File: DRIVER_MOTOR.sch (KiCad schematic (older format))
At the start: 14 parts, among them J7 MOT ARM, J8 MOT POLE, Q5 BC817, Q6 BC817, Q7 BC817, Q8 BC817

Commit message: cambiado a conectores MOLEX KK, agregados test points para señales analogicas
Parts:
- J3: renamed from J7; footprint Connector_JST:JST_EH_S3B-EH_1x03_P2.50mm_Horizontal -> Connector_Molex:Molex_KK-254_AE-6410-04A_1x04_P2.54mm_Vertical; symbol Connector_Generic:Conn_01x03 -> Connector_Generic:Conn_01x04
- J4: renamed from J8; footprint Connector_JST:JST_EH_S3B-EH_1x03_P2.50mm_Horizontal -> Connector_Molex:Molex_KK-254_AE-6410-04A_1x04_P2.54mm_Vertical; symbol Connector_Generic:Conn_01x03 -> Connector_Generic:Conn_01x04
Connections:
- wire segments 24 -> 30
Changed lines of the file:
@@
 $EndComp
 $Comp
-L Connector_Generic:Conn_01x03 J7
+L Connector_Generic:Conn_01x04 J3
 U 1 1 5F0F704A
-P 7050 1850
-F 0 "J7" H 7130 1892 50  0000 L CNN
-F 1 "MOT ARM" H 7130 1801 50  0000 L CNN
-F 2 "Connector_JST:JST_EH_S3B-EH_1x03_P2.50mm_Horizontal" H 7050 1850 50  0001 C CNN
-F 3 "~" H 7050 1850 50  0001 C CNN
-	1    7050 1850
+P 7050 1750
+F 0 "J3" H 7130 1792 50  0000 L CNN
+F 1 "MOT ARM" H 7130 1701 50  0000 L CNN
+F 2 "Connector_Molex:Molex_KK-254_AE-6410-04A_1x04_P2.54mm_Vertical" H 7050 1750 50  0001 C CNN
+F 3 "~" H 7050 1750 50  0001 C CNN
+	1    7050 1750
 	1    0    0    -1
 $EndComp
@@
 	5000 1850 6850 1850
 Wire Wire Line
-	6850 1950 6850 2400
-Wire Wire Line
-	6850 2400 6250 2400
+	6750 1950 6750 2400
 Connection ~ 6250 2400
 Wire Wire Line
@@
 $EndComp
 $Comp
-L Connector_Generic:Conn_01x03 J8
+L Connector_Generic:Conn_01x04 J4
 U 1 1 5F108145
-P 7050 3900
-F 0 "J8" H 7130 3942 50  0000 L CNN
-F 1 "MOT POLE" H 7130 3851 50  0000 L CNN
-F 2 "Connector_JST:JST_EH_S3B-EH_1x03_P2.50mm_Horizontal" H 7050 3900 50  0001 C CNN
-F 3 "~" H 7050 3900 50  0001 C CNN
-	1    7050 3900
+P 7050 3800
+F 0 "J4" H 7130 3842 50  0000 L CNN
+F 1 "MOT POLE" H 7130 3751 50  0000 L CNN
+F 2 "Connector_Molex:Molex_KK-254_AE-6410-04A_1x04_P2.54mm_Vertical" H 7050 3800 50  0001 C CNN
+F 3 "~" H 7050 3800 50  0001 C CNN
+	1    7050 3800
 	1    0    0    -1
 $EndComp
@@
 Wire Wire Line
 	5000 3900 6850 3900
-Wire Wire Line
-	6850 4000 6850 4450
-Wire Wire Line
-	6850 4450 6250 4450
 Connection ~ 6250 4450
 Wire Wire Line
 	6250 4450 6250 4500
+Wire Wire Line
+	6750 4450 6250 4450
+Wire Wire Line
+	6850 3700 6750 3700
+Wire Wire Line
+	6750 3700 6750 4000
+Wire Wire Line
+	6850 4000 6750 4000
+Connection ~ 6750 4000
+Wire Wire Line
+	6750 4000 6750 4450
+Wire Wire Line
+	6750 2400 6250 2400
+Wire Wire Line
+	6850 1950 6750 1950
+Wire Wire Line
+	6850 1650 6750 1650
+Wire Wire Line
+	6750 1650 6750 1950
+Connection ~ 6750 1950
 $EndSCHEMATC

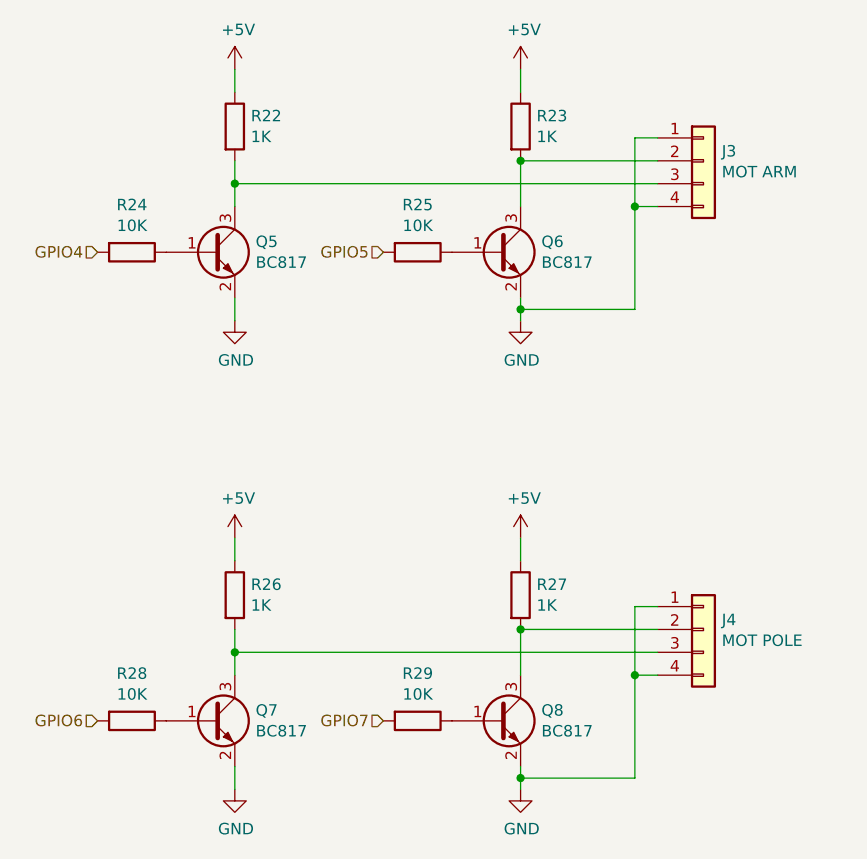
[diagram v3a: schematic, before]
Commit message: modificado cambiador de nivel de salida, agregados TP para los gpio STEP y DIRECTION de los motore PAP
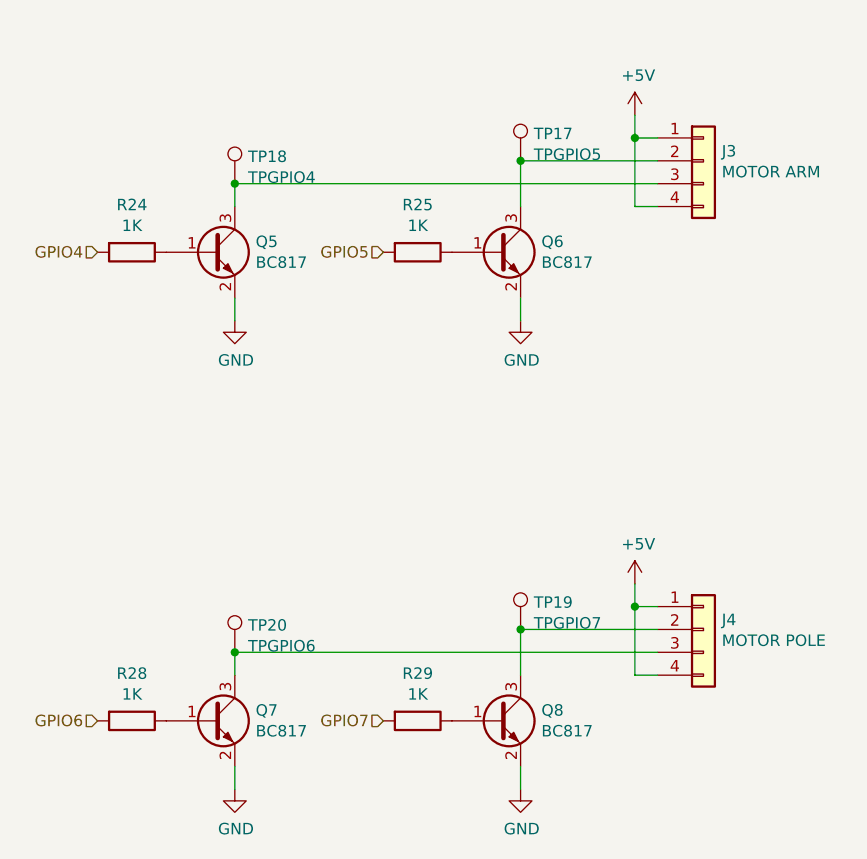
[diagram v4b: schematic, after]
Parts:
- removed R22, R23, R26, R27: 1K, Resistor_SMD:R_1206_3216Metric_Pad1.42x1.75mm_HandSolder, symbol Device:R
- added TP17: TPGPIO5, TestPoint:TestPoint_reducido, symbol Connector:TestPoint
- added TP18: TPGPIO4, TestPoint:TestPoint_reducido, symbol Connector:TestPoint
- added TP19: TPGPIO7, TestPoint:TestPoint_reducido, symbol Connector:TestPoint
- added TP20: TPGPIO6, TestPoint:TestPoint_reducido, symbol Connector:TestPoint
- J3: value MOT ARM -> MOTOR ARM
- J4: value MOT POLE -> MOTOR POLE
- R24, R25, R28, R29: value 10K -> 1K
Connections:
- net +5V: now also J3.1 (Pin_1), J3.4 (Pin_4), J4.1 (Pin_1), J4.4 (Pin_4)
- net GND: no longer J3.1 (Pin_1), J3.4 (Pin_4), J4.1 (Pin_1), J4.4 (Pin_4)
- net at J3.3 (Pin_3), Q5.3 (C): now also TP18.1
- net at J3.2 (Pin_2), Q6.3 (C): now also TP17.1
- net at J4.3 (Pin_3), Q7.3 (C): now also TP20.1
- net at J4.2 (Pin_2), Q8.3 (C): now also TP19.1
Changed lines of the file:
@@
 Wire Wire Line
 	5000 2350 5000 2450
-Wire Wire Line
-	5000 1350 5000 1450
 $Comp
 L power:GND #PWR051
@@
 P 4550 2150
 F 0 "R24" V 4343 2150 50  0000 C CNN
-F 1 "10K" V 4434 2150 50  0000 C CNN
+F 1 "1K" V 4434 2150 50  0000 C CNN
 F 2 "Resistor_SMD:R_1206_3216Metric_Pad1.42x1.75mm_HandSolder" V 4480 2150 50  0001 C CNN
 F 3 "~" H 4550 2150 50  0001 C CNN
 	1    4550 2150
 	0    1    1    0
-$EndComp
-$Comp
-L Device:R R22
-U 1 1 5F0E9734
-P 5000 1600
-F 0 "R22" H 5070 1646 50  0000 L CNN
-F 1 "1K" H 5070 1555 50  0000 L CNN
-F 2 "Resistor_SMD:R_1206_3216Metric_Pad1.42x1.75mm_HandSolder" V 4930 1600 50  0001 C CNN
-F 3 "~" H 5000 1600 50  0001 C CNN
-	1    5000 1600
-	1    0    0    -1
 $EndComp
 $Comp
@@
 $EndComp
 $Comp
-L power:+5V #PWR049
-U 1 1 5F0E76F8
-P 5000 1350
-F 0 "#PWR049" H 5000 1200 50  0001 C CNN
-F 1 "+5V" H 5015 1523 50  0000 C CNN
-F 2 "" H 5000 1350 50  0001 C CNN
-F 3 "" H 5000 1350 50  0001 C CNN
-	1    5000 1350
-	1    0    0    -1
-$EndComp
-$Comp
 L Connector_Generic:Conn_01x04 J3
 U 1 1 5F0F704A
 P 7050 1750
 F 0 "J3" H 7130 1792 50  0000 L CNN
-F 1 "MOT ARM" H 7130 1701 50  0000 L CNN
+F 1 "MOTOR ARM" H 7130 1701 50  0000 L CNN
 F 2 "Connector_Molex:Molex_KK-254_AE-6410-04A_1x04_P2.54mm_Vertical" H 7050 1750 50  0001 C CNN
 F 3 "~" H 7050 1750 50  0001 C CNN
@@
 $EndComp
 Wire Wire Line
-	6250 2350 6250 2400
-Wire Wire Line
-	6250 1350 6250 1450
+	6750 1550 6750 1650
 $Comp
 L power:GND #PWR052
@@
 P 5800 2150
 F 0 "R25" V 5593 2150 50  0000 C CNN
-F 1 "10K" V 5684 2150 50  0000 C CNN
+F 1 "1K" V 5684 2150 50  0000 C CNN
 F 2 "Resistor_SMD:R_1206_3216Metric_Pad1.42x1.75mm_HandSolder" V 5730 2150 50  0001 C CNN
 F 3 "~" H 5800 2150 50  0001 C CNN
 	1    5800 2150
 	0    1    1    0
-$EndComp
-$Comp
-L Device:R R23
-U 1 1 5F0FC0BA
-P 6250 1600
-F 0 "R23" H 6320 1646 50  0000 L CNN
-F 1 "1K" H 6320 1555 50  0000 L CNN
-F 2 "Resistor_SMD:R_1206_3216Metric_Pad1.42x1.75mm_HandSolder" V 6180 1600 50  0001 C CNN
-F 3 "~" H 6250 1600 50  0001 C CNN
-	1    6250 1600
-	1    0    0    -1
 $EndComp
 $Comp
@@
 L power:+5V #PWR050
 U 1 1 5F0FC0C6
-P 6250 1350
-F 0 "#PWR050" H 6250 1200 50  0001 C CNN
-F 1 "+5V" H 6265 1523 50  0000 C CNN
-F 2 "" H 6250 1350 50  0001 C CNN
-F 3 "" H 6250 1350 50  0001 C CNN
-	1    6250 1350
+P 6750 1550
+F 0 "#PWR050" H 6750 1400 50  0001 C CNN
+F 1 "+5V" H 6765 1723 50  0000 C CNN
+F 2 "" H 6750 1550 50  0001 C CNN
+F 3 "" H 6750 1550 50  0001 C CNN
+	1    6750 1550
 	1    0    0    -1
 $EndComp
 Wire Wire Line
 	6850 1750 6250 1750
-Connection ~ 6250 1750
-Wire Wire Line
-	5000 1750 5000 1850
-Connection ~ 5000 1850
 Wire Wire Line
 	5000 1850 5000 1950
@@
 	5000 1850 6850 1850
 Wire Wire Line
-	6750 1950 6750 2400
-Connection ~ 6250 2400
-Wire Wire Line
-	6250 2400 6250 2450
-Wire Wire Line
 	5000 4400 5000 4500
-Wire Wire Line
-	5000 3400 5000 3500
 $Comp
 L power:GND #PWR055
@@
 P 4550 4200
 F 0 "R28" V 4343 4200 50  0000 C CNN
-F 1 "10K" V 4434 4200 50  0000 C CNN
+F 1 "1K" V 4434 4200 50  0000 C CNN
 F 2 "Resistor_SMD:R_1206_3216Metric_Pad1.42x1.75mm_HandSolder" V 4480 4200 50  0001 C CNN
 F 3 "~" H 4550 4200 50  0001 C CNN
 	1    4550 4200
 	0    1    1    0
-$EndComp
-$Comp
-L Device:R R26
-U 1 1 5F108127
-P 5000 3650
-F 0 "R26" H 5070 3696 50  0000 L CNN
-F 1 "1K" H 5070 3605 50  0000 L CNN
-F 2 "Resistor_SMD:R_1206_3216Metric_Pad1.42x1.75mm_HandSolder" V 4930 3650 50  0001 C CNN
-F 3 "~" H 5000 3650 50  0001 C CNN
-	1    5000 3650
-	1    0    0    -1
 $EndComp
 $Comp
@@
 $EndComp
 $Comp
-L power:+5V #PWR053
-U 1 1 5F10813B
-P 5000 3400
-F 0 "#PWR053" H 5000 3250 50  0001 C CNN
-F 1 "+5V" H 5015 3573 50  0000 C CNN
-F 2 "" H 5000 3400 50  0001 C CNN
-F 3 "" H 5000 3400 50  0001 C CNN
-	1    5000 3400
-	1    0    0    -1
-$EndComp
-$Comp
 L Connector_Generic:Conn_01x04 J4
 U 1 1 5F108145
 P 7050 3800
 F 0 "J4" H 7130 3842 50  0000 L CNN
-F 1 "MOT POLE" H 7130 3751 50  0000 L CNN
+F 1 "MOTOR POLE" H 7130 3751 50  0000 L CNN
 F 2 "Connector_Molex:Molex_KK-254_AE-6410-04A_1x04_P2.54mm_Vertical" H 7050 3800 50  0001 C CNN
 F 3 "~" H 7050 3800 50  0001 C CNN
@@
 $EndComp
 Wire Wire Line
-	6250 4400 6250 4450
-Wire Wire Line
-	6250 3400 6250 3500
+	6750 3600 6750 3700
 $Comp
 L power:GND #PWR056
@@
 P 5800 4200
 F 0 "R29" V 5593 4200 50  0000 C CNN
-F 1 "10K" V 5684 4200 50  0000 C CNN
+F 1 "1K" V 5684 4200 50  0000 C CNN
 F 2 "Resistor_SMD:R_1206_3216Metric_Pad1.42x1.75mm_HandSolder" V 5730 4200 50  0001 C CNN
 F 3 "~" H 5800 4200 50  0001 C CNN
 	1    5800 4200
 	0    1    1    0
-$EndComp
-$Comp
-L Device:R R27
-U 1 1 5F108166
-P 6250 3650
-F 0 "R27" H 6320 3696 50  0000 L CNN
-F 1 "1K" H 6320 3605 50  0000 L CNN
-F 2 "Resistor_SMD:R_1206_3216Metric_Pad1.42x1.75mm_HandSolder" V 6180 3650 50  0001 C CNN
-F 3 "~" H 6250 3650 50  0001 C CNN
-	1    6250 3650
-	1    0    0    -1
 $EndComp
 $Comp
@@
 L power:+5V #PWR054
 U 1 1 5F10817A
-P 6250 3400
-F 0 "#PWR054" H 6250 3250 50  0001 C CNN
-F 1 "+5V" H 6265 3573 50  0000 C CNN
-F 2 "" H 6250 3400 50  0001 C CNN
-F 3 "" H 6250 3400 50  0001 C CNN
-	1    6250 3400
+P 6750 3600
+F 0 "#PWR054" H 6750 3450 50  0001 C CNN
+F 1 "+5V" H 6765 3773 50  0000 C CNN
+F 2 "" H 6750 3600 50  0001 C CNN
+F 3 "" H 6750 3600 50  0001 C CNN
+	1    6750 3600
 	1    0    0    -1
 $EndComp
 Wire Wire Line
 	6850 3800 6250 3800
+Wire Wire Line
+	5000 3900 5000 4000
+Wire Wire Line
+	6250 3800 6250 4000
+Wire Wire Line
+	5000 3900 6850 3900
+Wire Wire Line
+	6850 3700 6750 3700
+Wire Wire Line
+	6750 3700 6750 4000
+Wire Wire Line
+	6850 4000 6750 4000
+Wire Wire Line
+	6850 1950 6750 1950
+Wire Wire Line
+	6850 1650 6750 1650
+Wire Wire Line
+	6750 1650 6750 1950
+Connection ~ 6750 1650
+Wire Wire Line
+	6250 2350 6250 2450
+Connection ~ 6750 3700
+Wire Wire Line
+	6250 4400 6250 4500
+$Comp
+L Connector:TestPoint TP18
+U 1 1 5F24AB49
+P 5000 1850
+F 0 "TP18" H 5058 1968 50  0000 L CNN
+F 1 "TPGPIO4" H 5058 1877 50  0000 L CNN
+F 2 "TestPoint:TestPoint_reducido" H 5200 1850 50  0001 C CNN
+F 3 "~" H 5200 1850 50  0001 C CNN
+	1    5000 1850
+	1    0    0    -1
+$EndComp
+Connection ~ 5000 1850
+$Comp
+L Connector:TestPoint TP17
+U 1 1 5F24BAB9
+P 6250 1750
+F 0 "TP17" H 6308 1868 50  0000 L CNN
+F 1 "TPGPIO5" H 6308 1777 50  0000 L CNN
+F 2 "TestPoint:TestPoint_reducido" H 6450 1750 50  0001 C CNN
+F 3 "~" H 6450 1750 50  0001 C CNN
+	1    6250 1750
+	1    0    0    -1
+$EndComp
+Connection ~ 6250 1750
+$Comp
+L Connector:TestPoint TP20
+U 1 1 5F24C0E0
+P 5000 3900
+F 0 "TP20" H 5058 4018 50  0000 L CNN
+F 1 "TPGPIO6" H 5058 3927 50  0000 L CNN
+F 2 "TestPoint:TestPoint_reducido" H 5200 3900 50  0001 C CNN
+F 3 "~" H 5200 3900 50  0001 C CNN
+	1    5000 3900
+	1    0    0    -1
+$EndComp
+Connection ~ 5000 3900
+$Comp
+L Connector:TestPoint TP19
+U 1 1 5F24C53E
+P 6250 3800
+F 0 "TP19" H 6308 3918 50  0000 L CNN
+F 1 "TPGPIO7" H 6308 3827 50  0000 L CNN
+F 2 "TestPoint:TestPoint_reducido" H 6450 3800 50  0001 C CNN
+F 3 "~" H 6450 3800 50  0001 C CNN
+	1    6250 3800
+	1    0    0    -1
+$EndComp
 Connection ~ 6250 3800
-Wire Wire Line
-	5000 3800 5000 3900
-Connection ~ 5000 3900
-Wire Wire Line
-	5000 3900 5000 4000
-Wire Wire Line
-	6250 3800 6250 4000
-Wire Wire Line
-	5000 3900 6850 3900
-Connection ~ 6250 4450
-Wire Wire Line
-	6250 4450 6250 4500
-Wire Wire Line
-	6750 4450 6250 4450
-Wire Wire Line
-	6850 3700 6750 3700
-Wire Wire Line
-	6750 3700 6750 4000
-Wire Wire Line
-	6850 4000 6750 4000
-Connection ~ 6750 4000
-Wire Wire Line
-	6750 4000 6750 4450
-Wire Wire Line
-	6750 2400 6250 2400
-Wire Wire Line
-	6850 1950 6750 1950
-Wire Wire Line
-	6850 1650 6750 1650
-Wire Wire Line
-	6750 1650 6750 1950
-Connection ~ 6750 1950
 $EndSCHEMATC
